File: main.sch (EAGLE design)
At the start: 84 parts, among them Q1 5.8A/30V/35mΩ, Q2 5.8A/30V/35mΩ, Q3 2.5A/30V/105mΩ, U1 BQ24133_RGY_24, U2 SN65HVD32_D_8

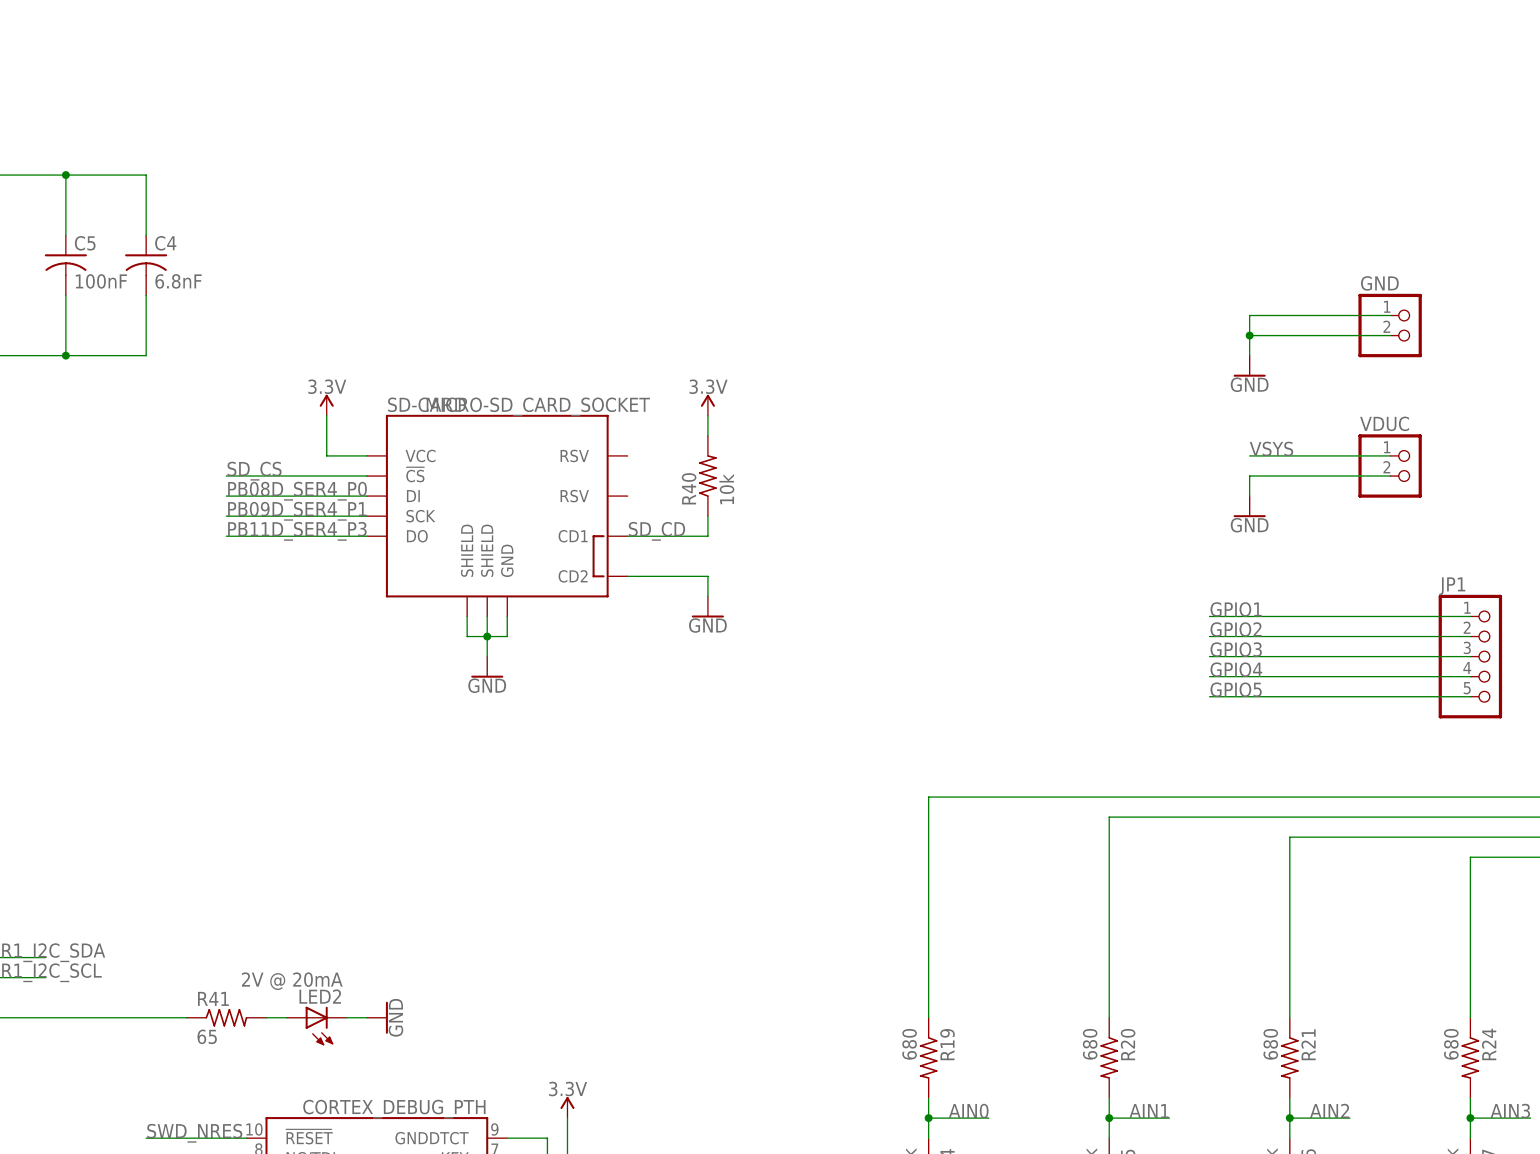
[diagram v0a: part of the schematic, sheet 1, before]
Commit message: Added leds, switched out SD card symbol and footprint
Couldn't find old footprint model # to actually order the part.
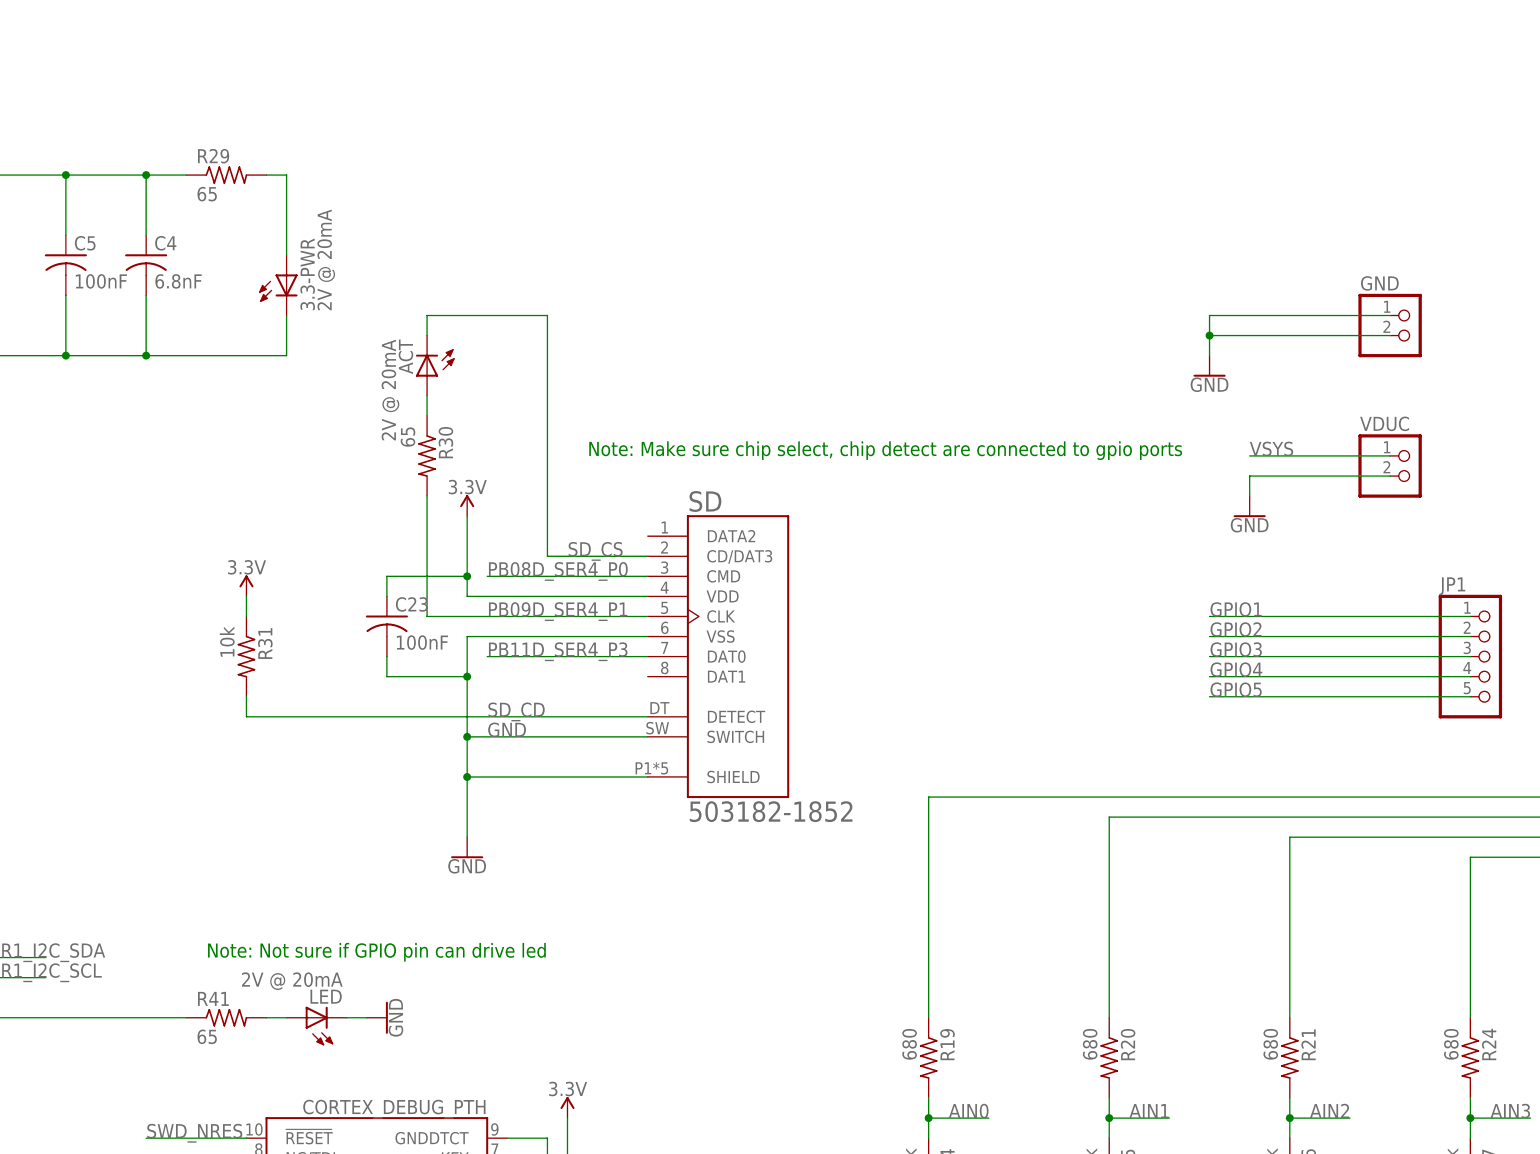
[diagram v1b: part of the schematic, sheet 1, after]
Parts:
- removed R40: 10k, resistor:R-US_R0603
- removed SD-CARD: MICRO-SD_CARD_SOCKET, SparkFun-Connectors:MICRO-SD_CARD_SOCKET
- added 3.3-PWR, ACT: 2V @ 20mA, adafruit:LEDCHIPLED_0603
- added C23: 100nF, resistor:C-USC0603
- added R29, R30: 65, resistor:R-US_R0603
- added R31: 10k, resistor:R-US_R0603
- added SD: 503182-1852, molex-microSD:503182-1852
- renumbered LED2 to LED, LED3 to CHG-STAT, R28 to GND-JMP
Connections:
- new net N$19: 3.3-PWR.A, R29.2
- new net N$20: ACT.A, R30.1
- net 3.3V: now also C23.1, R29.1, R31.1, SD.VDD; no longer R40.2, SD-CARD.VCC
- net GND: now also 3.3-PWR.C, C23.2, SD.SHIELD, SD.SWITCH, SD.VSS; no longer SD-CARD.CD2, SD-CARD.GND, SD-CARD.SHIELD@1, SD-CARD.SHIELD@3
- net PB08D_SER4_P0: now also SD.CMD; no longer SD-CARD.DI
- net PB09D_SER4_P1: now also R30.2, SD.CLK; no longer SD-CARD.SCK
- net PB11D_SER4_P3: now also SD.DAT0; no longer SD-CARD.DO
- net SD_CD: now also R31.2, SD.DETECT; no longer R40.1, SD-CARD.CD1
- net SD_CS: now also ACT.C, SD.CD/DAT3; no longer SD-CARD.!CS
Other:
- note added: "Note: Make sure chip select, chip detect are connected to gpio ports"
- note added: "Note: Not sure if GPIO pin can drive led"

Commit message: Routing
Working on finishing it up
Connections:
- net PC_SRN renamed BATT
- removed net N$7: D1.A1, Q1.D, R10.2, R8.2
- net AGND: now also C12.2, C15.2, C22.2, U1.PGND, U1.PGND_2
- net GND: no longer C12.2, C15.2, C22.2, U1.PGND, U1.PGND_2
- net VIN: now also D1.A1, Q1.D, R10.2, R8.2
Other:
- moved on the sheet: C15

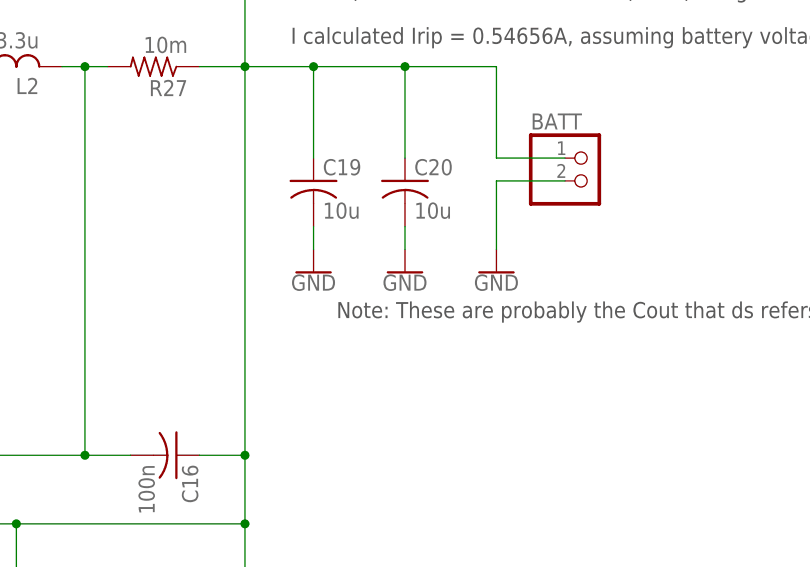
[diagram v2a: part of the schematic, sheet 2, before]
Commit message: Power
Ther are a few more things that I need to fix with power but this is the first prototype. I need to figure our how far away can D1 be from the battery imput before finilazing everything
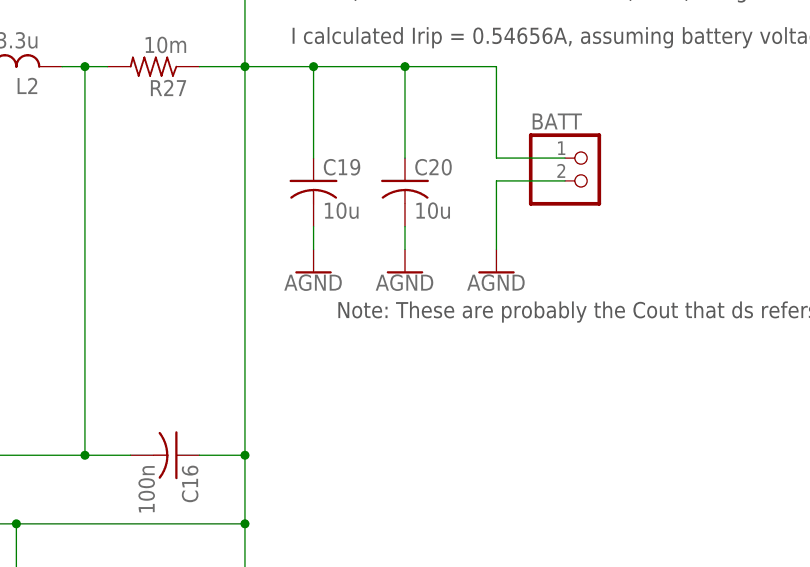
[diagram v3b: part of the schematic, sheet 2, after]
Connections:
- net AGND: now also BATT.2, C19.2, C20.2
- net GND: no longer BATT.2, C19.2, C20.2
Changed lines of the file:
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@@
 <part name="C19" library="rcl" library_urn="urn:adsk.eagle:library:334" deviceset="C-US" device="C1206" package3d_urn="urn:adsk.eagle:package:23618/2" value="10u"/>
 <part name="C20" library="rcl" library_urn="urn:adsk.eagle:library:334" deviceset="C-US" device="C1206" package3d_urn="urn:adsk.eagle:package:23618/2" value="10u"/>
-<part name="GND31" library="SparkFun-PowerSymbols" deviceset="GND" device=""/>
-<part name="GND32" library="SparkFun-PowerSymbols" deviceset="GND" device=""/>
 <part name="BATT" library="pinhead" library_urn="urn:adsk.eagle:library:325" deviceset="PINHD-1X2" device="" package3d_urn="urn:adsk.eagle:package:22435/2"/>
-<part name="GND33" library="SparkFun-PowerSymbols" deviceset="GND" device=""/>
 <part name="SUPPLY7" library="SparkFun-PowerSymbols" deviceset="3.3V" device=""/>
 <part name="AIN" library="pinhead" library_urn="urn:adsk.eagle:library:325" deviceset="PINHD-1X5" device="" package3d_urn="urn:adsk.eagle:package:22469/2"/>
@@
 <part name="U$19" library="SparkFun-PowerSymbols" deviceset="AGND" device=""/>
 <part name="U$20" library="SparkFun-PowerSymbols" deviceset="AGND" device=""/>
+<part name="U$22" library="SparkFun-PowerSymbols" deviceset="AGND" device=""/>
+<part name="U$23" library="SparkFun-PowerSymbols" deviceset="AGND" device=""/>
+<part name="U$24" library="SparkFun-PowerSymbols" deviceset="AGND" device=""/>
 </parts>
 <sheets>
@@
 <instance part="C19" gate="G$1" x="515.62" y="81.28"/>
 <instance part="C20" gate="G$1" x="525.78" y="81.28"/>
-<instance part="GND31" gate="1" x="515.62" y="71.12"/>
-<instance part="GND32" gate="1" x="525.78" y="71.12"/>
 <instance part="BATT" gate="G$1" x="546.1" y="81.28"/>
-<instance part="GND33" gate="1" x="535.94" y="71.12"/>
 <instance part="S2" gate="1" x="530.86" y="147.32"/>
 <instance part="U1" gate="A" x="403.86" y="109.22" smashed="yes">
@@
 <instance part="U$19" gate="G$1" x="340.36" y="116.84"/>
 <instance part="U$20" gate="G$1" x="490.22" y="119.38"/>
+<instance part="U$22" gate="G$1" x="535.94" y="71.12"/>
+<instance part="U$23" gate="G$1" x="525.78" y="71.12"/>
+<instance part="U$24" gate="G$1" x="515.62" y="71.12"/>
 </instances>
 <busses>
@@
 <pinref part="GND7" gate="1" pin="GND"/>
 <pinref part="C7" gate="G$1" pin="2"/>
-</segment>
-<segment>
-<pinref part="C19" gate="G$1" pin="2"/>
-<pinref part="GND31" gate="1" pin="GND"/>
-<wire x1="515.62" y1="73.66" x2="515.62" y2="76.2" width="0.1524" layer="91"/>
-</segment>
-<segment>
-<pinref part="C20" gate="G$1" pin="2"/>
-<pinref part="GND32" gate="1" pin="GND"/>
-<wire x1="525.78" y1="76.2" x2="525.78" y2="73.66" width="0.1524" layer="91"/>
-</segment>
-<segment>
-<pinref part="BATT" gate="G$1" pin="2"/>
-<wire x1="543.56" y1="81.28" x2="535.94" y2="81.28" width="0.1524" layer="91"/>
-<wire x1="535.94" y1="81.28" x2="535.94" y2="73.66" width="0.1524" layer="91"/>
-<pinref part="GND33" gate="1" pin="GND"/>
 </segment>
 <segment>
@@
 <pinref part="U$20" gate="G$1" pin="AGND"/>
 </segment>
-</net>
+<segment>
+<pinref part="BATT" gate="G$1" pin="2"/>
+<wire x1="543.56" y1="81.28" x2="535.94" y2="81.28" width="0.1524" layer="91"/>
+<wire x1="535.94" y1="81.28" x2="535.94" y2="73.66" width="0.1524" layer="91"/>
+<pinref part="U$22" gate="G$1" pin="AGND"/>
+</segment>
+<segment>
+<pinref part="C20" gate="G$1" pin="2"/>
+<wire x1="525.78" y1="76.2" x2="525.78" y2="73.66" width="0.1524" layer="91"/>
+<pinref part="U$23" gate="G$1" pin="AGND"/>
+</segment>
+<segment>
+<pinref part="C19" gate="G$1" pin="2"/>
+<wire x1="515.62" y1="73.66" x2="515.62" y2="76.2" width="0.1524" layer="91"/>
+<pinref part="U$24" gate="G$1" pin="AGND"/>
+</segment>
+</net>

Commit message: Some layout stuff, package changes
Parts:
- removed 3.3-PWR, ACT, LED: 2V @ 20mA, adafruit:LEDCHIPLED_0603
- removed JP1: (no value), pinhead:PINHD-1X5
- removed R29, R30: 65, resistor:R-US_R0603
- added GPIO: (no value), pinhead:PINHD-1X10
- added LED0, LED1: 2V @ 20mA, adafruit:LEDCHIPLED_0603
- added R28: 64.9, resistor:R-US_R0603
- C10, C11, C12, C14, C15, C18, C19, C20, C21, C25: device rcl:C-USC1206 -> resistor:C-USC0603
- R14, R15, R16, R17, R18: value 1.32k -> ?
- R19, R20, R21, R24, R25: value 680 -> ?
- R41, R42: value 65 -> 64.9
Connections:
- removed net LED: MCU.PA19(SER1:3+), R41.1
- removed net N$29: LED.A, R41.2
- removed net VOS: C6.1, L1.2, R3.2, TPS62162-Q1.VOS
- new net GPIO10: GPIO.10
- new net GPIO6: GPIO.6
- new net GPIO7: GPIO.7
- new net GPIO8: GPIO.8
- new net GPIO9: GPIO.9
- new net N$7: LED0.C, R41.2
- net 3.3V: now also C6.1, L1.2, LED0.A, LED1.A, R3.2, TPS62162-Q1.VOS; no longer R29.1
- net GND: no longer 3.3-PWR.C, LED.C
- net GPIO1: now also GPIO.1; no longer JP1.1
- net GPIO2: now also GPIO.2; no longer JP1.2
- net GPIO3: now also GPIO.3; no longer JP1.3
- net GPIO4: now also GPIO.4; no longer JP1.4
- net GPIO5: now also GPIO.5; no longer JP1.5
- net N$19: now also SD.CD/DAT3; no longer 3.3-PWR.A, R29.2
- net N$20: now also LED1.C, R28.2; no longer ACT.A, R30.1
- net PB09D_SER4_P1: no longer R30.2
- net SD_CS: no longer ACT.C, SD.CD/DAT3
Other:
- note added: "CAUTION: NEED to know source(ducers) impedance before picking voltage divider resistor values. Also the samd21 adc has a maximum source impedance of 3.5kohms."
- note removed: "Note: Not sure if GPIO pin can drive led"
- moved on the sheet: AIN, R14, R15, R16, R17, R18, R19, R20, R21, R24, R25, R41
